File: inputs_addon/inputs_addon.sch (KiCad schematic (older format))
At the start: 19 parts, among them J1 Conn_01x14_Female, J2 Conn_01x14_Male, SW1 SW_Push, SW2 SW_Push

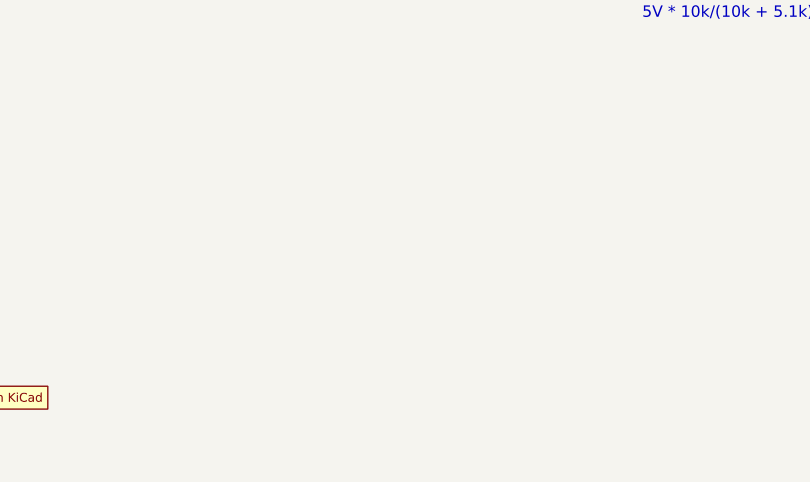
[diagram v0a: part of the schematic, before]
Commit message: switch to vertical headers, add mounting holes
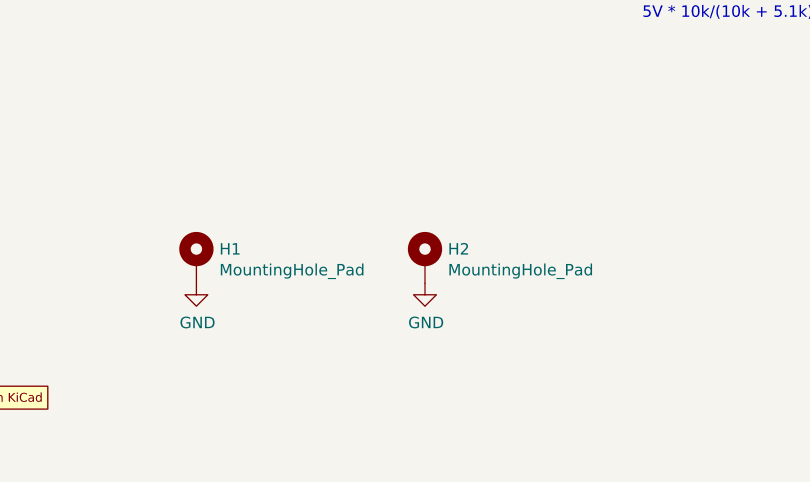
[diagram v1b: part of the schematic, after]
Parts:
- added H1, H2: MountingHole_Pad, MountingHole:MountingHole_3.2mm_M3_Pad, symbol Mechanical:MountingHole_Pad
- J1: footprint Connector_PinSocket_2.54mm:PinSocket_1x14_P2.54mm_Horizontal -> Connector_PinSocket_2.54mm:PinSocket_1x14_P2.54mm_Vertical
- J2: footprint Connector_PinHeader_2.54mm:PinHeader_1x14_P2.54mm_Horizontal -> Connector_PinHeader_2.54mm:PinHeader_1x14_P2.54mm_Vertical
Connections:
- net GND: now also H1.1, H2.1
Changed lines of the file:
@@
 F 0 "J1" H 2542 3635 50  0000 C CNN
 F 1 "Conn_01x14_Female" H 2542 3544 50  0000 C CNN
-F 2 "Connector_PinSocket_2.54mm:PinSocket_1x14_P2.54mm_Horizontal" H 2650 2850 50  0001 C CNN
+F 2 "Connector_PinSocket_2.54mm:PinSocket_1x14_P2.54mm_Vertical" H 2650 2850 50  0001 C CNN
 F 3 "~" H 2650 2850 50  0001 C CNN
 	1    2650 2850
@@
 F 0 "J2" H 9672 2824 50  0000 R CNN
 F 1 "Conn_01x14_Male" H 9672 2733 50  0000 R CNN
-F 2 "Connector_PinHeader_2.54mm:PinHeader_1x14_P2.54mm_Horizontal" H 9700 2850 50  0001 C CNN
+F 2 "Connector_PinHeader_2.54mm:PinHeader_1x14_P2.54mm_Vertical" H 9700 2850 50  0001 C CNN
 F 3 "~" H 9700 2850 50  0001 C CNN
 	1    9700 2850
@@
 	1    0    0    -1
 $EndComp
+$Comp
+L Mechanical:MountingHole_Pad H1
+U 1 1 5E1D47F3
+P 4050 6950
+F 0 "H1" H 4150 6999 50  0000 L CNN
+F 1 "MountingHole_Pad" H 4150 6908 50  0000 L CNN
+F 2 "MountingHole:MountingHole_3.2mm_M3_Pad" H 4050 6950 50  0001 C CNN
+F 3 "~" H 4050 6950 50  0001 C CNN
+	1    4050 6950
+	1    0    0    -1
+$EndComp
+$Comp
+L power:GND #PWR?
+U 1 1 5E1D4C44
+P 4050 7050
+F 0 "#PWR?" H 4050 6800 50  0001 C CNN
+F 1 "GND" H 4055 6877 50  0000 C CNN
+F 2 "" H 4050 7050 50  0001 C CNN
+F 3 "" H 4050 7050 50  0001 C CNN
+	1    4050 7050
+	1    0    0    -1
+$EndComp
+$Comp
+L Mechanical:MountingHole_Pad H2
+U 1 1 5E1D5FD6
+P 5050 6950
+F 0 "H2" H 5150 6999 50  0000 L CNN
+F 1 "MountingHole_Pad" H 5150 6908 50  0000 L CNN
+F 2 "MountingHole:MountingHole_3.2mm_M3_Pad" H 5050 6950 50  0001 C CNN
+F 3 "~" H 5050 6950 50  0001 C CNN
+	1    5050 6950
+	1    0    0    -1
+$EndComp
+$Comp
+L power:GND #PWR?
+U 1 1 5E1D5FDC
+P 5050 7050
+F 0 "#PWR?" H 5050 6800 50  0001 C CNN
+F 1 "GND" H 5055 6877 50  0000 C CNN
+F 2 "" H 5050 7050 50  0001 C CNN
+F 3 "" H 5050 7050 50  0001 C CNN
+	1    5050 7050
+	1    0    0    -1
+$EndComp
